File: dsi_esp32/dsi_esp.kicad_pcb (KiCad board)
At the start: 2 copper layers, 27.6 x 60 mm, 16 parts, among them U1 ndsPADS, U2 ESP32-S3-WROOM-1

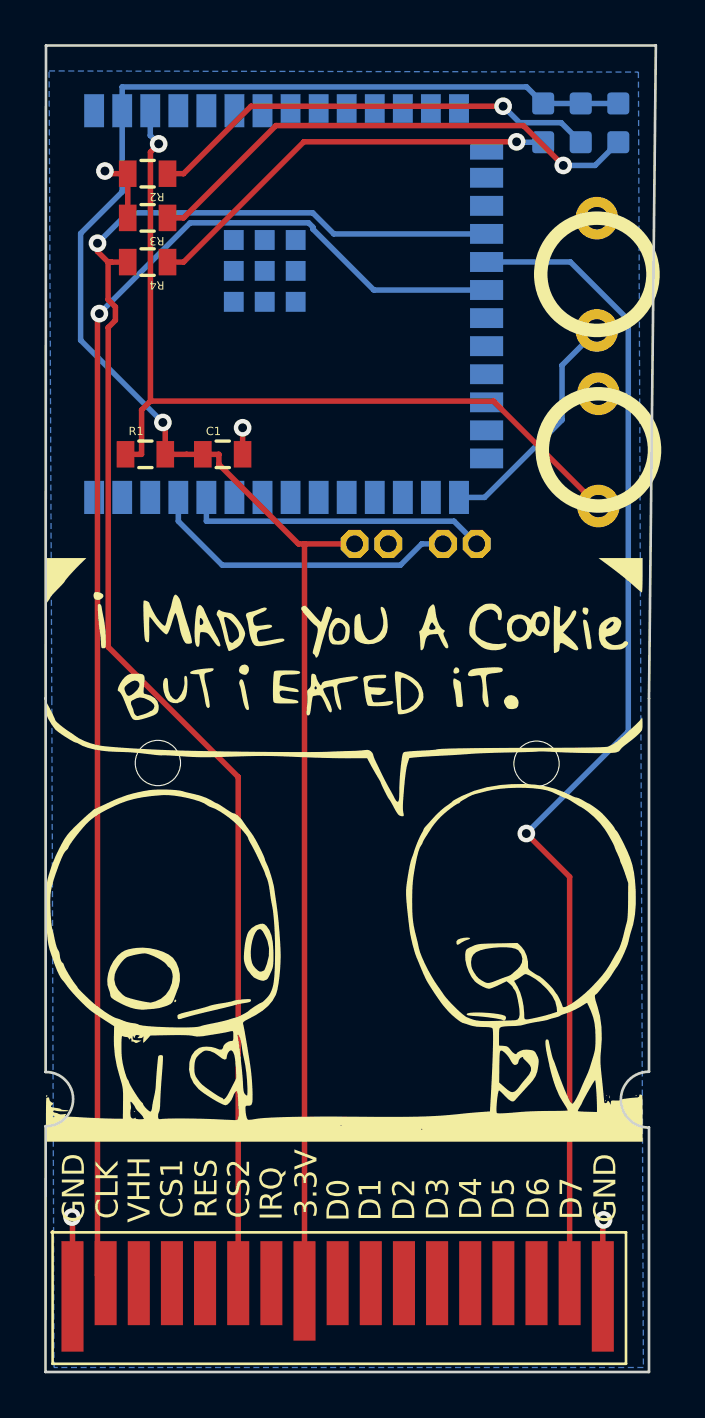
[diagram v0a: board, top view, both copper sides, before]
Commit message: working prototype that sends the images automatically over esp-now and is able to display. esp-now is too slow however so we need to switch from it
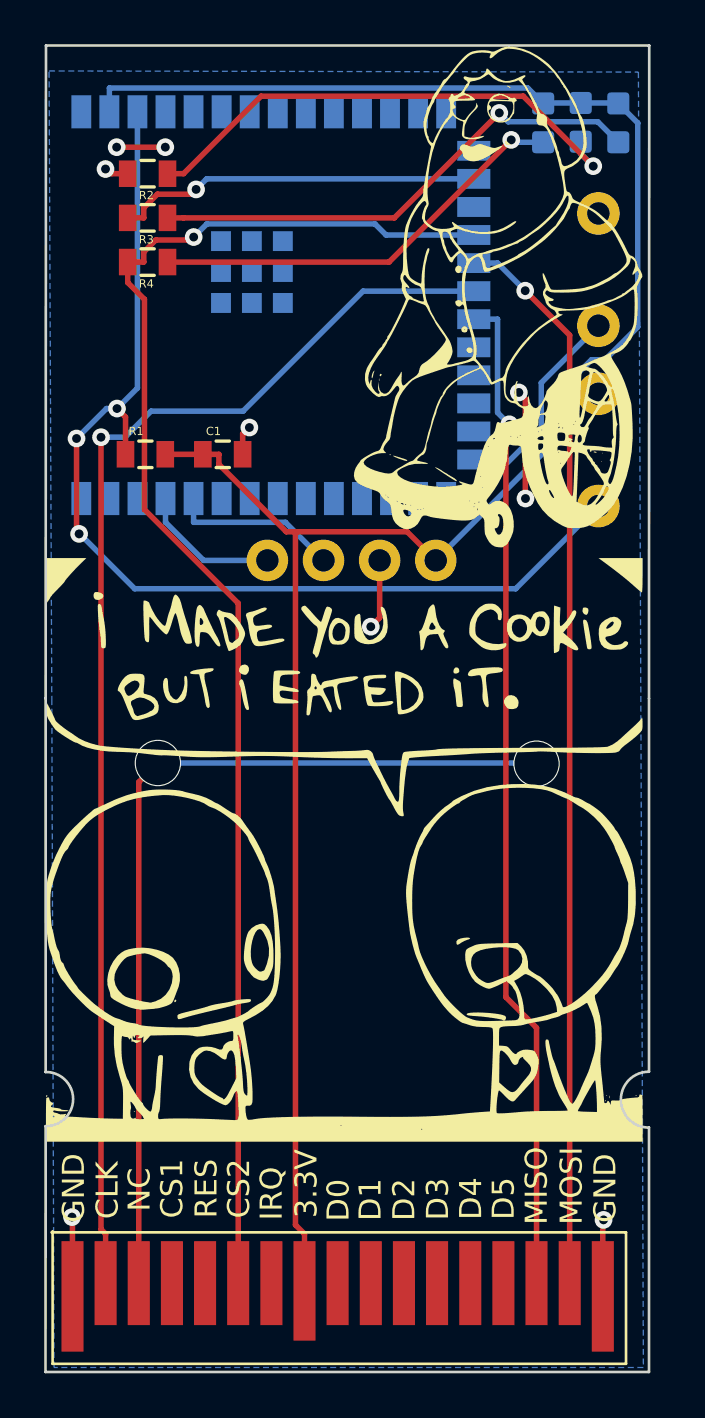
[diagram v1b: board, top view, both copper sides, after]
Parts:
- removed G***: LOGO, LOGO
- removed POWER: RED, Ilya_Teach:LED-0603
- removed POWER1, PROGRAM1: ~, Ilya_Teach:1X2_SMALL_TH
- added J1: ~, SparkFun-Connectors:1X04, B.Cu at (133.8, 63.5)
- added POWER2: RED, Ilya_Teach:LED-0603, B.Cu at (140.4, 43.7)
- added joe: LOGO, LOGO, F.Cu at (136.5, 50.5)
- added up: LOGO, LOGO, B.Cu at (129.8, 83.1)
- BOOT1, RESET1: moved to B.Cu
- moved U2 0.58 mm to (126.1, 52.0)
- moved BOOT1 0.22 mm to (141.2, 50.3)
- renumbered G*** to cookie
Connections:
- R3 pad 2: /GND -> /WIFI_IND
- U1 pad 15: unconnected-(U1-D6-Pad15) -> /SPI_MISO
- U2 pad 16: unconnected-(U2-GPIO46-Pad16) -> /WIFI_IND
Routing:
- net /SPI_MISO: track 0.00 -> 45.6 mm, vias 0 -> 1
- net unconnected-(U1-UNUSED-Pad3): track 0.07 -> 41.0 mm
- net /WIFI_IND: track 0.00 -> 16.7 mm, vias 0 -> 1
- net /VCC: track 86.1 -> 98.6 mm, vias 1 -> 0
- net Net-(RESET1-1): track 39.0 -> 48.9 mm, vias 1 -> 3
- net /TXD: track 14.3 -> 6.40 mm
- net /GND: track 13.4 -> 20.1 mm, vias 4 -> 9
- net /SPI_CLK: track 64.6 -> 58.0 mm
- net /RXD: track 13.7 -> 7.67 mm
- net /SPI_MOSI: track 53.8 -> 48.6 mm
- net /SPI_CS: track 69.4 -> 65.1 mm
- net Net-(POWER2-PadA): track 20.6 -> 23.4 mm
- net Net-(BOOT1-1): track 10.8 -> 11.3 mm
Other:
- board size 27.6 x 60 mm -> 27.3 x 60 mm
- board text added: "MISO"
- board text added: "MOSI"
- board text added: "NC"
- board text added: "RX"
- board text added: "TX"
- board text added: "V"
- board text removed: "D6"
- board text removed: "D7"
- board text removed: "TX RX"
- board text removed: "V GND"
- board text removed: "VHH"
